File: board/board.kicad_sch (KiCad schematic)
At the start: 82 parts, among them IC1 tps610981dser, IC2 LTR-303ALS-01, IC3 EFM32TG108F32-D-QFN24, J1 Conn_01x05_Male, J2 , J3 , J4 , Q1 Q_PMOS_GSD, Q2 Q_PMOS_GSD

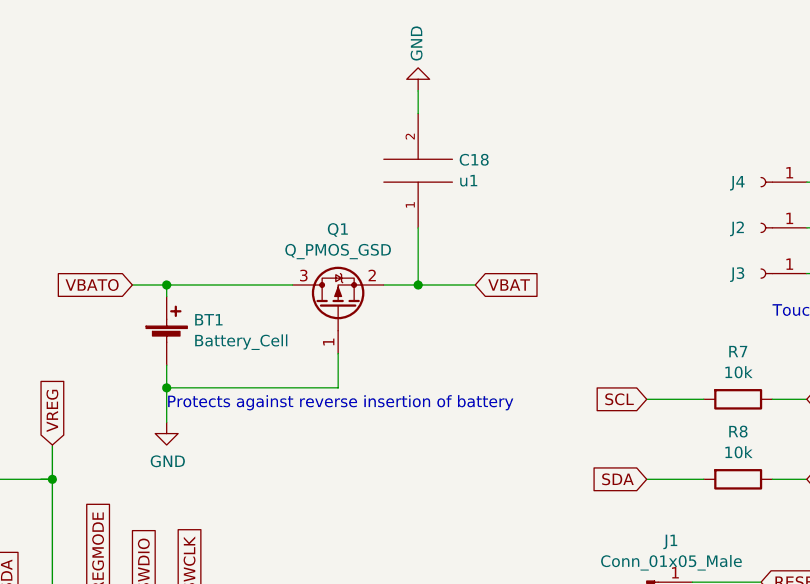
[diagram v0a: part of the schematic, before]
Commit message: switch to using glider for battery holder
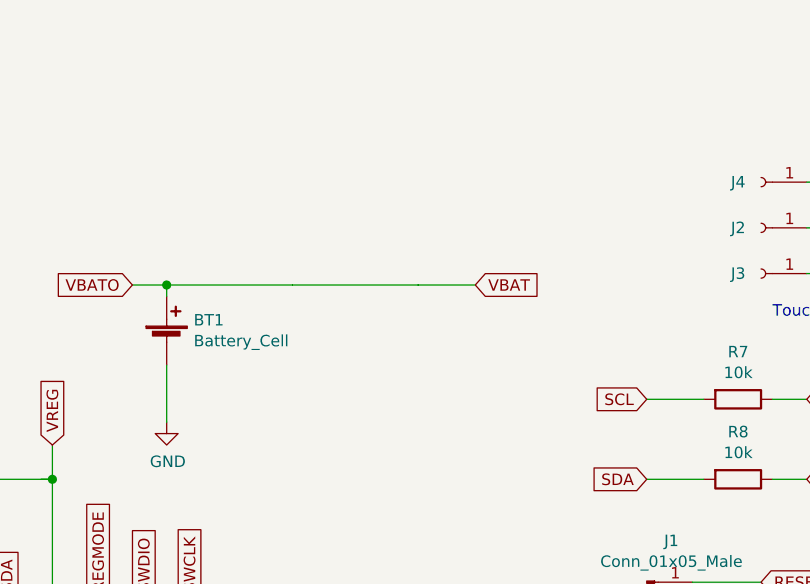
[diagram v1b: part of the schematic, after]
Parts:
- removed C18: u1, mlm:0603, symbol pspice:CAP
- removed Q1: Q_PMOS_GSD, Package_TO_SOT_SMD:SOT-23, symbol Device:Q_PMOS_GSD
- BT1: footprint mlm:BK-5067 -> mlm:BHX1-2032-SM
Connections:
- net VBATO is gone; now on net VBAT: BT1.1 (+)
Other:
- note removed: "Protects against reverse insertion of battery"
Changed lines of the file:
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@@
   (junction (at 187.96 154.94) (diameter 1.016) (color 0 0 0 0))
   (junction (at 200.66 31.75) (diameter 1.016) (color 0 0 0 0))
-  (junction (at 200.66 43.18) (diameter 1.016) (color 0 0 0 0))
   (junction (at 203.2 140.97) (diameter 1.016) (color 0 0 0 0))
   (junction (at 203.2 154.94) (diameter 1.016) (color 0 0 0 0))
   (junction (at 219.71 93.98) (diameter 1.016) (color 0 0 0 0))
-  (junction (at 228.6 31.75) (diameter 1.016) (color 0 0 0 0))
   (junction (at 237.49 104.14) (diameter 1.016) (color 0 0 0 0))
   (junction (at 251.46 104.14) (diameter 1.016) (color 0 0 0 0))
-  (no_connect (at 193.04 129.54))
-  (no_connect (at 198.12 129.54))
+  (no_connect (at 27.94 227.33))
+  (no_connect (at 138.43 158.75))
   (no_connect (at 41.91 227.33))
-  (no_connect (at 41.91 217.17))
   (no_connect (at 27.94 217.17))
+  (no_connect (at 193.04 129.54))
+  (no_connect (at 198.12 129.54))
   (no_connect (at 35.56 234.95))
-  (no_connect (at 138.43 158.75))
-  (no_connect (at 27.94 227.33))
+  (no_connect (at 41.91 217.17))
   (wire (pts (xy 3.81 167.64) (xy 6.35 167.64))
     (stroke (width 0) (type solid) (color 0 0 0 0))
@@
     (stroke (width 0) (type solid) (color 0 0 0 0))
   )
-  (wire (pts (xy 200.66 40.64) (xy 200.66 43.18))
-    (stroke (width 0) (type solid) (color 0 0 0 0))
-  )
-  (wire (pts (xy 200.66 43.18) (xy 200.66 46.99))
+  (wire (pts (xy 200.66 40.64) (xy 200.66 46.99))
     (stroke (width 0) (type solid) (color 0 0 0 0))
   )
@@
     (stroke (width 0) (type solid) (color 0 0 0 0))
   )
+  (wire (pts (xy 214.63 31.75) (xy 228.6 31.75))
+    (stroke (width 0) (type solid) (color 0 0 0 0))
+  )
   (wire (pts (xy 218.44 78.74) (xy 223.52 78.74))
     (stroke (width 0) (type solid) (color 0 0 0 0))
@@
     (stroke (width 0) (type solid) (color 0 0 0 0))
   )
-  (wire (pts (xy 219.71 43.18) (xy 200.66 43.18))
-    (stroke (width 0) (type solid) (color 0 0 0 0))
-  )
-  (wire (pts (xy 219.71 43.18) (xy 219.71 39.37))
-    (stroke (width 0) (type solid) (color 0 0 0 0))
-  )
   (wire (pts (xy 219.71 93.98) (xy 219.71 72.39))
     (stroke (width 0) (type solid) (color 0 0 0 0))
@@
     (stroke (width 0) (type solid) (color 0 0 0 0))
   )
-  (wire (pts (xy 224.79 31.75) (xy 228.6 31.75))
-    (stroke (width 0) (type solid) (color 0 0 0 0))
-  )
-  (wire (pts (xy 228.6 10.16) (xy 228.6 12.7))
-    (stroke (width 0) (type solid) (color 0 0 0 0))
-  )
-  (wire (pts (xy 228.6 25.4) (xy 228.6 31.75))
-    (stroke (width 0) (type solid) (color 0 0 0 0))
-  )
   (wire (pts (xy 228.6 31.75) (xy 234.95 31.75))
     (stroke (width 0) (type solid) (color 0 0 0 0))
@@
     (stroke (width 0) (type solid) (color 0 0 0 0))
   )
-  (text "Protects against reverse insertion of battery" (at 200.66 45.72 0)
-    (effects (font (size 1.27 1.27)) (justify left bottom))
-  )
   (text "Programming/debug header" (at 256.54 80.01 0)
     (effects (font (size 1.27 1.27)) (justify left bottom))
@@
     )
   )
-  (symbol (lib_id "power:GND") (at 228.6 10.16 180) (unit 1)
-    (in_bom yes) (on_board yes)
-    (property "Reference" "#PWR02" (id 0) (at 228.6 3.81 0)
-      (effects (font (size 1.27 1.27)) hide)
-    )
-    (property "Value" "GND" (id 1) (at 228.473 6.9088 90)
-      (effects (font (size 1.27 1.27)) (justify right))
-    )
-    (property "Footprint" "" (id 2) (at 228.6 10.16 0)
-      (effects (font (size 1.27 1.27)) hide)
-    )
-    (property "Datasheet" "" (id 3) (at 228.6 10.16 0)
-      (effects (font (size 1.27 1.27)) hide)
-    )
-  )
   (symbol (lib_id "power:GND") (at 237.49 134.62 0) (unit 1)
     (in_bom yes) (on_board yes)
@@
       (effects (font (size 1.27 1.27)) (justify left))
     )
-    (property "Footprint" "mlm:BK-5067" (id 2) (at 200.66 36.576 90)
+    (property "Footprint" "mlm:BHX1-2032-SM" (id 2) (at 200.66 36.576 90)
       (effects (font (size 1.27 1.27)) hide)
     )
@@
     )
   )
-  (symbol (lib_name "pspice:CAP_1") (lib_id "pspice:CAP") (at 228.6 19.05 180) (unit 1)
-    (in_bom yes) (on_board yes)
-    (property "Reference" "C18" (id 0) (at 233.1212 17.8816 0)
-      (effects (font (size 1.27 1.27)) (justify right))
-    )
-    (property "Value" "u1" (id 1) (at 233.1212 20.193 0)
-      (effects (font (size 1.27 1.27)) (justify right))
-    )
-    (property "Footprint" "mlm:0603" (id 2) (at 228.6 19.05 0)
-      (effects (font (size 1.27 1.27)) hide)
-    )
-    (property "Datasheet" "~" (id 3) (at 228.6 19.05 0)
-      (effects (font (size 1.27 1.27)) hide)
-    )
-    (property "MPN" "885012206020" (id 4) (at 228.6 19.05 0)
-      (effects (font (size 1.27 1.27)) hide)
-    )
-    (property "MAN" "Wurth Elektronik" (id 5) (at 228.6 19.05 0)
-      (effects (font (size 1.27 1.27)) hide)
-    )
-  )
   (symbol (lib_name "pspice:CAP_17") (lib_id "pspice:CAP") (at 237.49 120.65 180) (unit 1)
     (in_bom yes) (on_board yes)
@@
     )
   )
-  (symbol (lib_id "Device:Q_PMOS_GSD") (at 219.71 34.29 90) (unit 1)
-    (in_bom yes) (on_board yes)
-    (property "Reference" "Q1" (id 0) (at 219.71 25.5778 90))
-    (property "Value" "Q_PMOS_GSD" (id 1) (at 219.71 27.8892 90))
-    (property "Footprint" "Package_TO_SOT_SMD:SOT-23" (id 2) (at 217.17 29.21 0)
-      (effects (font (size 1.27 1.27)) hide)
-    )
-    (property "Datasheet" "~" (id 3) (at 219.71 34.29 0)
-      (effects (font (size 1.27 1.27)) hide)
-    )
-    (property "MPN" "SI2329DS-T1-GE3" (id 4) (at 219.71 34.29 90)
-      (effects (font (size 1.27 1.27)) hide)
-    )
-    (property "MAN" "Vishay" (id 5) (at 219.71 34.29 90)
-      (effects (font (size 1.27 1.27)) hide)
-    )
-  )
   (symbol (lib_id "mlm:LTR303ALS01") (at 128.27 156.21 0) (unit 1)
     (in_bom yes) (on_board yes)
@@
       (reference "#PWR01") (unit 1) (value "GND") (footprint "")
     )
-    (path "/068e0490-b0a4-4ec1-9333-f3bf614a504e"
-      (reference "#PWR02") (unit 1) (value "GND") (footprint "")
-    )
     (path "/f129fde2-5fb5-4219-a8b2-f1461d9154b2"
       (reference "#PWR03") (unit 1) (value "GND") (footprint "")
@@
     )
     (path "/1eb174aa-9dd7-4231-a34f-62df98ce6f8b"
-      (reference "BT1") (unit 1) (value "Battery_Cell") (footprint "mlm:BK-5067")
+      (reference "BT1") (unit 1) (value "Battery_Cell") (footprint "mlm:BHX1-2032-SM")
     )
     (path "/cf55fafc-e904-492f-a59c-c6054a833ef5"
@@
       (reference "C17") (unit 1) (value "u1") (footprint "mlm:0603")
     )
-    (path "/a1b87259-c524-4efd-8871-edeb738e5b5a"
-      (reference "C18") (unit 1) (value "u1") (footprint "mlm:0603")
-    )
     (path "/265f1272-c35c-44b2-bc61-a449afef1ad3"
       (reference "C19") (unit 1) (value "1u") (footprint "mlm:0603")
@@
       (reference "MH5") (unit 1) (value "Screw thread") (footprint "mlm:97730306330R")
     )
-    (path "/6c9d9de8-0fba-4586-8e69-d598e24323a4"
-      (reference "Q1") (unit 1) (value "Q_PMOS_GSD") (footprint "Package_TO_SOT_SMD:SOT-23")
-    )
     (path "/48c96cd8-6530-4d51-a3ce-670704f17856"

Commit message: more work on glider; cap changes
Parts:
- removed C15, C2: 10u, mlm:0603, symbol pspice:CAP
- C16, C3: value 10u -> 47u; MAN Taiyo Yuden -> Murata Electronics; MPN JMK107ABJ106MA-T -> GRM188R60G476ME15D
- C17: value u1 -> 1u; MAN Wurth Elektronik -> Samsung Electro-Mechanics; MPN 885012206020 -> CL10B105KP8NNNC
- C19: MAN Wurth Elektronik -> Samsung Electro-Mechanics
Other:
- moved on the sheet: C16, C17, C3

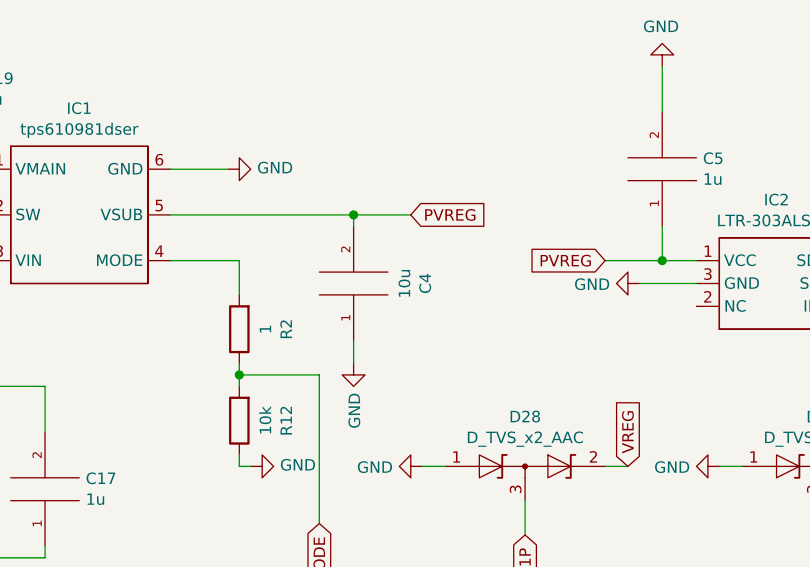
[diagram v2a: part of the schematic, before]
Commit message: reduce ldo output cap
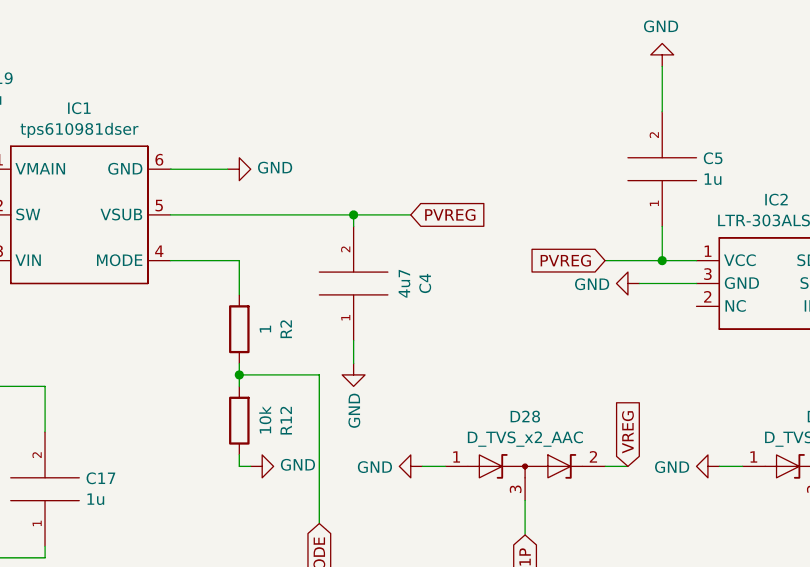
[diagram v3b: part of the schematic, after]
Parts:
- C4: value 10u -> 4u7; MAN Taiyo Yuden -> Samsung Electro-Mechanics; MPN JMK107ABJ106MA-T -> C0603C475K9PAC7411
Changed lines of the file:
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@@
   (junction (at 237.49 104.14) (diameter 1.016) (color 0 0 0 0))
   (junction (at 251.46 104.14) (diameter 1.016) (color 0 0 0 0))
-  (no_connect (at 27.94 217.17))
-  (no_connect (at 198.12 129.54))
-  (no_connect (at 41.91 227.33))
-  (no_connect (at 138.43 158.75))
-  (no_connect (at 35.56 234.95))
-  (no_connect (at 27.94 227.33))
   (no_connect (at 41.91 217.17))
   (no_connect (at 193.04 129.54))
+  (no_connect (at 35.56 234.95))
+  (no_connect (at 27.94 217.17))
+  (no_connect (at 27.94 227.33))
+  (no_connect (at 41.91 227.33))
+  (no_connect (at 198.12 129.54))
+  (no_connect (at 138.43 158.75))
   (wire (pts (xy 8.89 167.64) (xy 20.32 167.64))
     (stroke (width 0) (type solid) (color 0 0 0 0))
@@
     (in_bom yes) (on_board yes)
     (property "Reference" "C4" (id 0) (at 90.551 156.21 90))
-    (property "Value" "10u" (id 1) (at 88.2396 156.21 90))
+    (property "Value" "4u7" (id 1) (at 88.2396 156.21 90))
     (property "Footprint" "mlm:0603" (id 2) (at 82.55 156.21 0)
       (effects (font (size 1.27 1.27)) hide)
@@
       (effects (font (size 1.27 1.27)) hide)
     )
-    (property "MPN" "JMK107ABJ106MA-T" (id 4) (at 82.55 156.21 90)
-      (effects (font (size 1.27 1.27)) hide)
-    )
-    (property "MAN" "Taiyo Yuden" (id 5) (at 82.55 156.21 90)
+    (property "MPN" "C0603C475K9PAC7411" (id 4) (at 82.55 156.21 90)
+      (effects (font (size 1.27 1.27)) hide)
+    )
+    (property "MAN" "Samsung Electro-Mechanics" (id 5) (at 82.55 156.21 90)
       (effects (font (size 1.27 1.27)) hide)
     )
@@
     )
     (path "/cbfb5810-7add-4af9-9915-d14fc62eb3e0"
-      (reference "C4") (unit 1) (value "10u") (footprint "mlm:0603")
+      (reference "C4") (unit 1) (value "4u7") (footprint "mlm:0603")
     )
     (path "/2f677b12-9362-4312-a1be-6f38f913537a"

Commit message: fix some mpn metadata
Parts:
- BT1: MAN Keystone -> Memory Protection Devices; MPN 3002 -> BHX1-2032-SM
- J1: MPN (none) -> M20-7910542R
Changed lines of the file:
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@@
   (junction (at 237.49 104.14) (diameter 1.016) (color 0 0 0 0))
   (junction (at 251.46 104.14) (diameter 1.016) (color 0 0 0 0))
+  (no_connect (at 193.04 129.54))
+  (no_connect (at 41.91 227.33))
+  (no_connect (at 138.43 158.75))
   (no_connect (at 41.91 217.17))
-  (no_connect (at 193.04 129.54))
   (no_connect (at 35.56 234.95))
   (no_connect (at 27.94 217.17))
+  (no_connect (at 198.12 129.54))
   (no_connect (at 27.94 227.33))
-  (no_connect (at 41.91 227.33))
-  (no_connect (at 198.12 129.54))
-  (no_connect (at 138.43 158.75))
   (wire (pts (xy 8.89 167.64) (xy 20.32 167.64))
     (stroke (width 0) (type solid) (color 0 0 0 0))
@@
       (effects (font (size 1.27 1.27)) hide)
     )
-    (property "MPN" "3002" (id 4) (at -8.89 64.77 0)
-      (effects (font (size 1.27 1.27)) hide)
-    )
-    (property "MAN" "Keystone" (id 5) (at 200.66 38.1 0)
+    (property "MPN" "BHX1-2032-SM" (id 4) (at -8.89 64.77 0)
+      (effects (font (size 1.27 1.27)) hide)
+    )
+    (property "MAN" "Memory Protection Devices" (id 5) (at 200.66 38.1 0)
       (effects (font (size 1.27 1.27)) hide)
     )
@@
       (effects (font (size 1.27 1.27)) hide)
     )
+    (property "MPN" "M20-7910542R" (id 5) (at 254 69.85 0)
+      (effects (font (size 1.27 1.27)) hide)
+    )

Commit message: final tweaks to pcb
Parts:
- BT1: footprint mlm:BHX1-2032-SM -> mlm:BK-5067; MPN BHX1-2032-SM -> BK-5067
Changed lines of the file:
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@@
   (junction (at 237.49 104.14) (diameter 1.016) (color 0 0 0 0))
   (junction (at 251.46 104.14) (diameter 1.016) (color 0 0 0 0))
+  (no_connect (at 27.94 227.33))
+  (no_connect (at 41.91 217.17))
   (no_connect (at 193.04 129.54))
   (no_connect (at 41.91 227.33))
   (no_connect (at 138.43 158.75))
-  (no_connect (at 41.91 217.17))
   (no_connect (at 35.56 234.95))
   (no_connect (at 27.94 217.17))
   (no_connect (at 198.12 129.54))
-  (no_connect (at 27.94 227.33))
   (wire (pts (xy 8.89 167.64) (xy 20.32 167.64))
     (stroke (width 0) (type solid) (color 0 0 0 0))
@@
       (effects (font (size 1.27 1.27)) (justify left))
     )
-    (property "Footprint" "mlm:BHX1-2032-SM" (id 2) (at 200.66 36.576 90)
+    (property "Footprint" "mlm:BK-5067" (id 2) (at 200.66 36.576 90)
       (effects (font (size 1.27 1.27)) hide)
     )
@@
       (effects (font (size 1.27 1.27)) hide)
     )
-    (property "MPN" "BHX1-2032-SM" (id 4) (at -8.89 64.77 0)
+    (property "MPN" "BK-5067" (id 4) (at -8.89 64.77 0)
       (effects (font (size 1.27 1.27)) hide)
     )
@@
     )
     (path "/1eb174aa-9dd7-4231-a34f-62df98ce6f8b"
-      (reference "BT1") (unit 1) (value "Battery_Cell") (footprint "mlm:BHX1-2032-SM")
+      (reference "BT1") (unit 1) (value "Battery_Cell") (footprint "mlm:BK-5067")
     )
     (path "/cf55fafc-e904-492f-a59c-c6054a833ef5"
